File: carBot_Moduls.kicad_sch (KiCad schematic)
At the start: 12 parts, among them J1 Batt_1, J2 Batt_2, J3 Conn_MOT_FL, J4 Conn_MOT_RL, J5 Conn_MOT_FR, J6 Conn_MOT_RR, SW1 SW_SPST

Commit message: Add all modules
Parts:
- added BZ1: Buzzer, symbol Device:Buzzer
- added D1: 1N4148, Diode_THT:D_DO-35_SOD27_P7.62mm_Horizontal, symbol Diode:1N4148
- added J10: IR_sensor, symbol Connector_Generic:Conn_01x03
- added J11: RGB_LED_B, symbol Connector_Generic:Conn_01x03
- added J7: UltraSonic, symbol Connector_Generic:Conn_01x04
- added J8: RGB_LED_F, symbol Connector_Generic:Conn_01x03
- added J9: OLED, symbol Connector_Generic:Conn_01x04
- added Q1: BC547, Package_TO_SOT_THT:TO-92_Inline, symbol Transistor_BJT:BC547
- added R1, R3: 330, symbol Device:R
- added R2: 1K, symbol Device:R
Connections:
- net +5V: now also BZ1.1 (+), D1.1 (K), J11.2 (Pin_2), J8.2 (Pin_2)
- net 3.3V: now also J10.1 (Pin_1), J7.1 (Pin_1), J9.2 (Pin_2)
- net GND: now also J10.2 (Pin_2), J11.3 (Pin_3), J7.4 (Pin_4), J8.3 (Pin_3), J9.1 (Pin_1), Q1.3 (E)
- net SONAR_ECHO: now also J7.3 (Pin_3)
- net SONAR_TRIG: now also J7.2 (Pin_2)
- net IR_DATA: now reaches U1.31 (Pin_31)
- net IR_DATA: now also J10.3 (Pin_3)
- net OLED_SDA: now reaches U1.33 (Pin_33)
- net OLED_SDA: now also J9.4 (Pin_4)
- net OLED_SCL: now reaches U1.36 (Pin_36)
- net OLED_SCL: now also J9.3 (Pin_3)
- net Buzzer_EN: now reaches U1.37 (Pin_37)
- net Buzzer_EN: now also R2.1
- net LED_DATA_B: now reaches U1.7 (Pin_7)
- net LED_DATA_B: now also R3.1
- net LED_DATA renamed LED_DATA_F
- net LED_DATA_F: now also R1.1
- new net: Q1.2 (B), R2.2
- new net: J11.1 (Pin_1), R3.2
- new net: J8.1 (Pin_1), R1.2
- new net: BZ1.2 (-), D1.2 (A), Q1.1 (C)
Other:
- moved on the sheet: C1, J1, J2, J3, J4, J5, J6, SW1, U1, U2, U3, U4

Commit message: Add files via upload
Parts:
- added J12: Conn_01x06, CarBotLibrary:TP4056_TypeC_Module, symbol Connector_Generic:Conn_01x06
- U1: footprint (none) -> CarBotLibrary:ESP32-38pins
- U2: footprint (none) -> CarBotLibrary:Buck
- U3: footprint (none) -> CarBotLibrary:BMS
- U4: footprint (none) -> CarBotLibrary:MotDriver
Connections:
- no-connect marks 0 -> 1
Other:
- moved on the sheet: J10, J9
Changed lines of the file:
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@@
 		(color 0 0 0 0)
 	)
+	(no_connect
+		(at 45.72 74.93)
+	)
 	(wire
 		(pts
@@
 	(wire
 		(pts
-			(xy 230.505 151.13) (xy 233.68 151.13)
+			(xy 231.14 135.89) (xy 234.315 135.89)
 		)
 		(stroke
@@
 	(wire
 		(pts
-			(xy 230.505 153.67) (xy 233.68 153.67)
-		)
-		(stroke
-			(width 0)
-			(type default)
-		)
-	)
-	(wire
-		(pts
-			(xy 230.505 148.59) (xy 233.68 148.59)
+			(xy 231.14 138.43) (xy 234.315 138.43)
+		)
+		(stroke
+			(width 0)
+			(type default)
+		)
+	)
+	(wire
+		(pts
+			(xy 231.14 133.35) (xy 234.315 133.35)
 		)
 		(stroke
@@
 	)
 	(label "IR_DATA"
-		(at 230.505 153.67 180)
+		(at 231.14 138.43 180)
 		(effects
 			(font
@@
 	)
 	(label "GND"
-		(at 230.505 151.13 180)
+		(at 231.14 135.89 180)
 		(effects
 			(font
@@
 	)
 	(label "OLED_SCL"
-		(at 233.68 136.525 180)
+		(at 234.315 121.285 180)
 		(effects
 			(font
@@
 	)
 	(label "3.3V"
-		(at 233.68 133.985 180)
+		(at 234.315 118.745 180)
 		(effects
 			(font
@@
 	)
 	(label "GND"
-		(at 233.68 131.445 180)
+		(at 234.315 116.205 180)
 		(effects
 			(font
@@
 		)
 	)
-	(label "DIN"
-		(at 28.575 73.025 180)
-		(effects
-			(font
-				(size 1.27 1.27)
-			)
-			(justify right bottom)
-		)
-	)
 	(label "3.3V"
-		(at 230.505 148.59 180)
+		(at 231.14 133.35 180)
 		(effects
 			(font
@@
 	)
 	(label "OLED_SDA"
-		(at 233.68 139.065 180)
+		(at 234.315 123.825 180)
 		(effects
 			(font
@@
 	)
 	(symbol
+		(lib_id "Connector_Generic:Conn_01x06")
+		(at 191.135 139.7 0)
+		(unit 1)
+		(exclude_from_sim no)
+		(in_bom yes)
+		(on_board yes)
+		(dnp no)
+		(fields_autoplaced yes)
+		(property "Reference" "J12"
+			(at 194.31 139.6999 0)
+			(effects
+				(font
+					(size 1.27 1.27)
+				)
+				(justify left)
+			)
+		)
+		(property "Value" "Conn_01x06"
+			(at 194.31 142.2399 0)
+			(effects
+				(font
+					(size 1.27 1.27)
+				)
+				(justify left)
+			)
+		)
+		(property "Footprint" "CarBotLibrary:TP4056_TypeC_Module"
+			(at 191.135 139.7 0)
+			(effects
+				(font
+					(size 1.27 1.27)
+				)
+				(hide yes)
+			)
+		)
+		(property "Datasheet" "~"
+			(at 191.135 139.7 0)
+			(effects
+				(font
+					(size 1.27 1.27)
+				)
+				(hide yes)
+			)
+		)
+		(property "Description" "Generic connector, single row, 01x06, script generated (kicad-library-utils/schlib/autogen/connector/)"
+			(at 191.135 139.7 0)
+			(effects
+				(font
+					(size 1.27 1.27)
+				)
+				(hide yes)
+			)
+		)
+		(pin "4"
+		)
+		(pin "2"
+		)
+		(pin "1"
+		)
+		(pin "3"
+		)
+		(pin "5"
+		)
+		(pin "6"
+		)
+		(instances
+			(project ""
+				(path "/df05b431-47a2-405b-9491-3f7c618e89eb"
+					(reference "J12")
+					(unit 1)
+				)
+			)
+		)
+	)
+	(symbol
 		(lib_id "Device:R")
 		(at 144.145 102.87 90)
@@
 			)
 		)
-		(property "Footprint" ""
+		(property "Footprint" "CarBotLibrary:MotDriver"
 			(at 154.305 44.45 0)
 			(effects
@@
 			)
 		)
-		(property "Footprint" ""
+		(property "Footprint" "CarBotLibrary:ESP32-38pins"
 			(at 62.23 29.845 0)
 			(effects
@@
 	(symbol
 		(lib_id "Connector_Generic:Conn_01x03")
-		(at 238.76 151.13 0)
+		(at 239.395 135.89 0)
 		(unit 1)
 		(exclude_from_sim no)
@@
 		(fields_autoplaced yes)
 		(property "Reference" "J10"
-			(at 241.935 149.8599 0)
+			(at 242.57 134.6199 0)
 			(effects
 				(font
@@
 		)
 		(property "Value" "IR_sensor"
-			(at 241.935 152.3999 0)
+			(at 242.57 137.1599 0)
 			(effects
 				(font
@@
 		)
 		(property "Footprint" ""
-			(at 238.76 151.13 0)
+			(at 239.395 135.89 0)
 			(effects
 				(font
@@
 		)
 		(property "Datasheet" "~"
-			(at 238.76 151.13 0)
+			(at 239.395 135.89 0)
 			(effects
 				(font
@@
 		)
 		(property "Description" "Generic connector, single row, 01x03, script generated (kicad-library-utils/schlib/autogen/connector/)"
-			(at 238.76 151.13 0)
+			(at 239.395 135.89 0)
 			(effects
 				(font
@@
 	(symbol
 		(lib_id "Connector_Generic:Conn_01x04")
-		(at 238.76 133.985 0)
+		(at 239.395 118.745 0)
 		(unit 1)
 		(exclude_from_sim no)
@@
 		(fields_autoplaced yes)
 		(property "Reference" "J9"
-			(at 241.3 133.9849 0)
+			(at 241.935 118.7449 0)
 			(effects
 				(font
@@
 		)
 		(property "Value" "OLED"
-			(at 241.3 136.5249 0)
+			(at 241.935 121.2849 0)
 			(effects
 				(font
@@
 		)
 		(property "Footprint" ""
-			(at 238.76 133.985 0)
+			(at 239.395 118.745 0)
 			(effects
 				(font
@@
 		)
 		(property "Datasheet" "~"
-			(at 238.76 133.985 0)
+			(at 239.395 118.745 0)
 			(effects
 				(font
@@
 		)
 		(property "Description" "Generic connector, single row, 01x04, script generated (kicad-library-utils/schlib/autogen/connector/)"
-			(at 238.76 133.985 0)
+			(at 239.395 118.745 0)
 			(effects
 				(font
@@
 			)
 		)
-		(property "Footprint" ""
+		(property "Footprint" "CarBotLibrary:BMS"
 			(at 213.36 17.145 0)
 			(effects
@@
 					(size 1.27 1.27)
 				)
-			)
-		)
-		(property "Footprint" ""
+				(hide yes)
+			)
+		)
+		(property "Footprint" "CarBotLibrary:Buck"
 			(at 172.72 18.415 0)
 			(effects

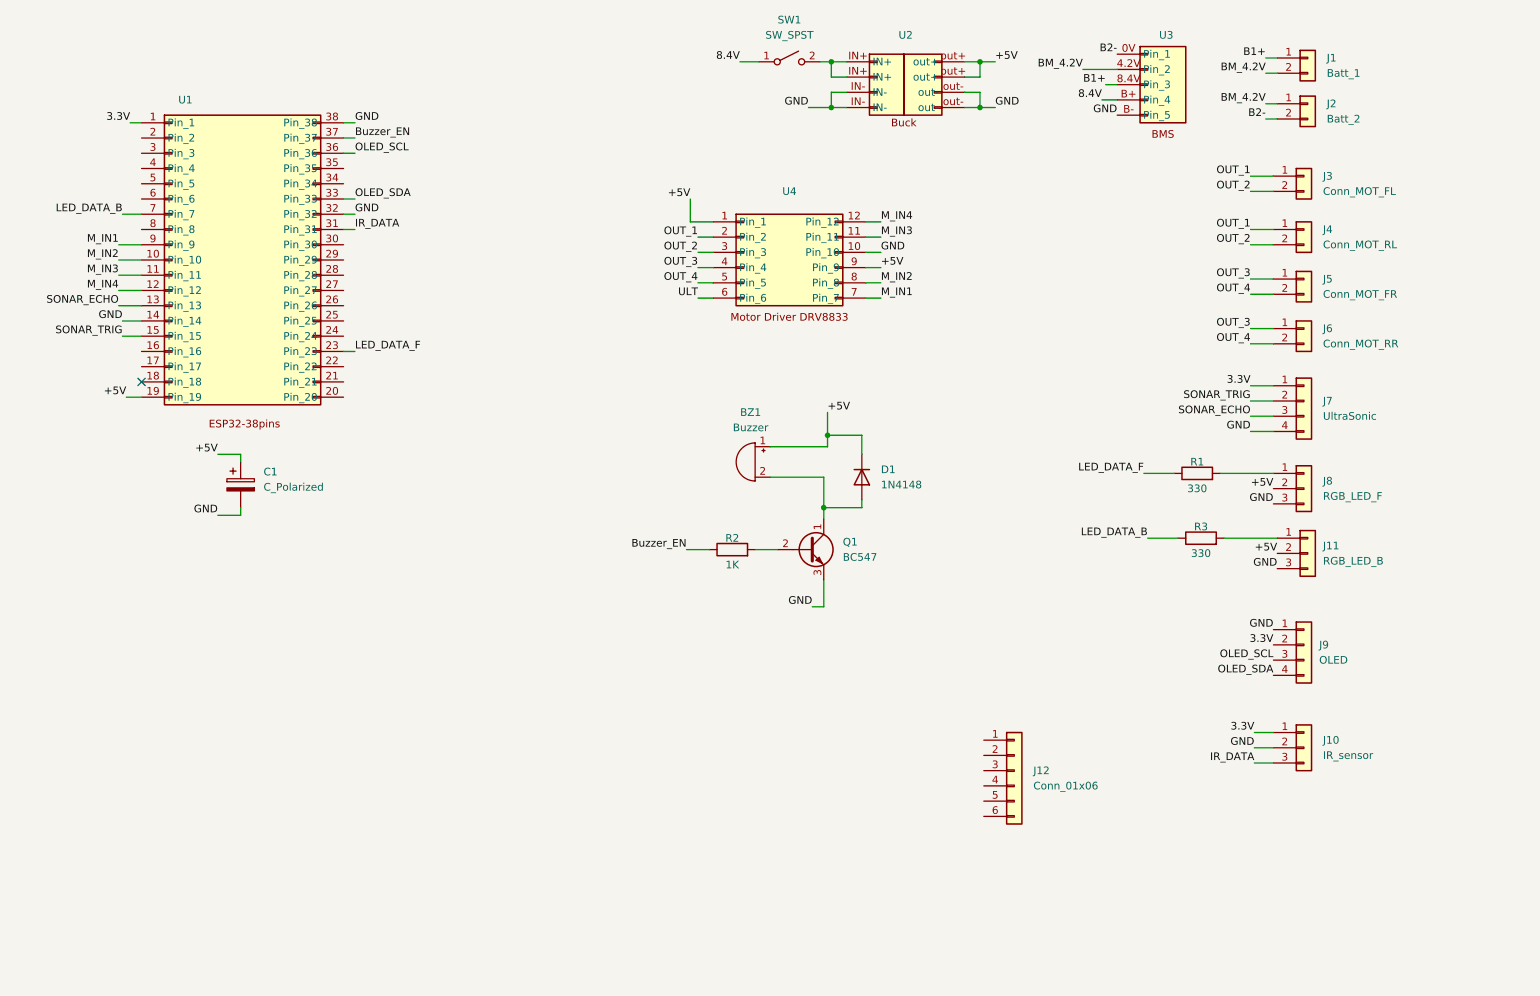
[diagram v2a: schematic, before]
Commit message: assgin footprint
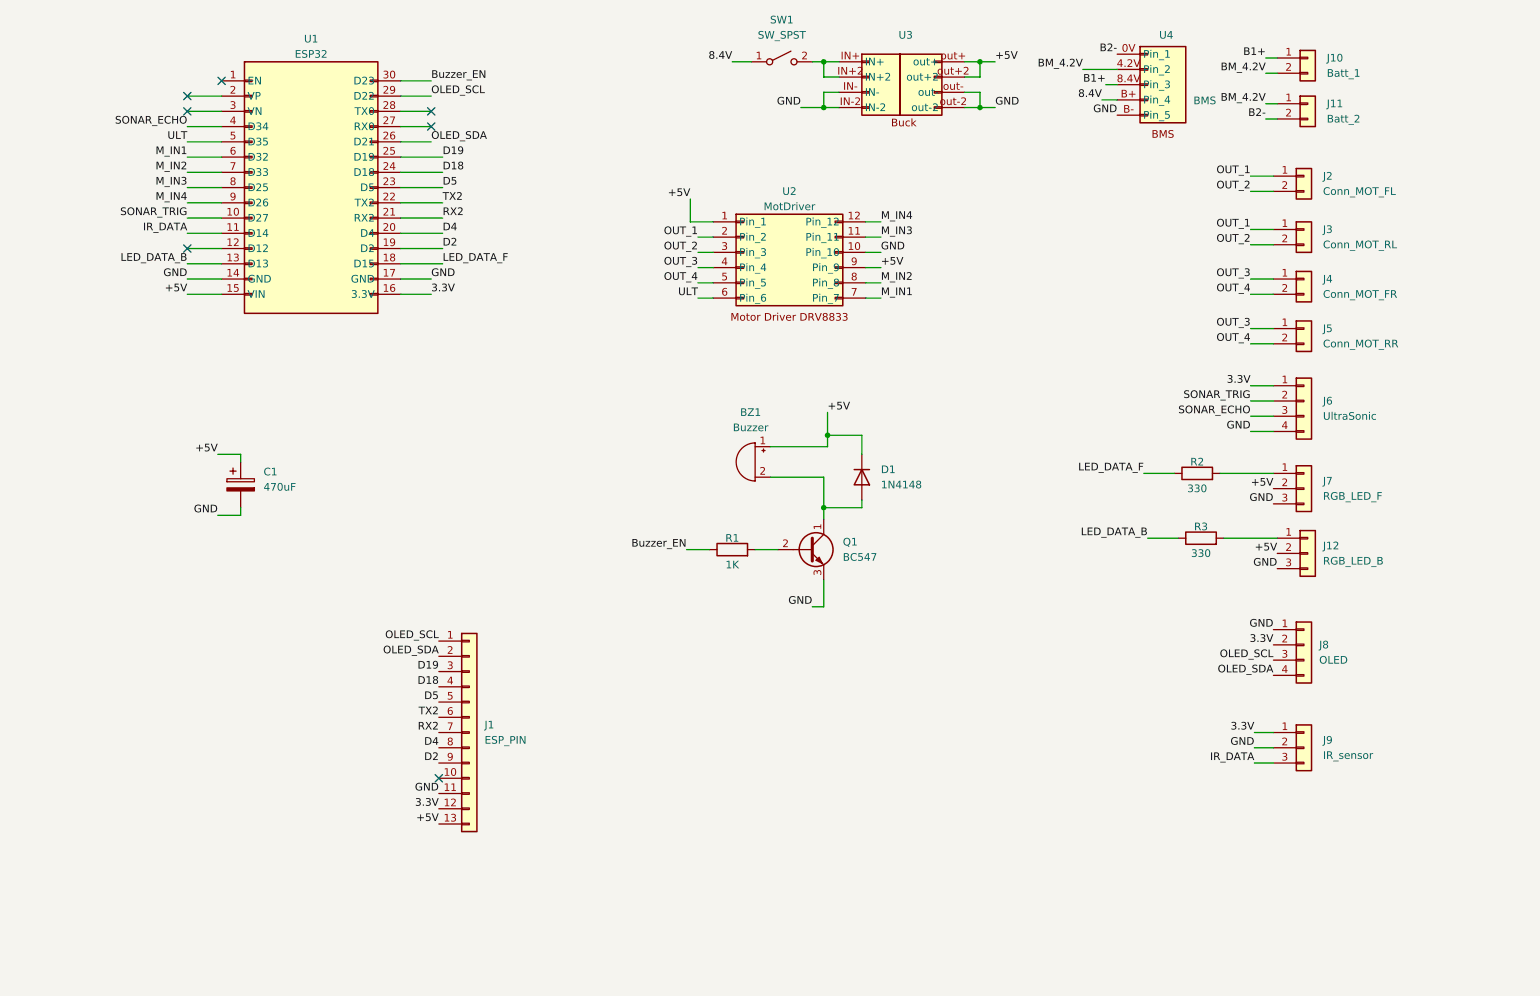
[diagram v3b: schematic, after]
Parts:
- removed J12: Conn_01x06, CarBotLibrary:TP4056_TypeC_Module, symbol Connector_Generic:Conn_01x06
- removed U1: ~, CarBotLibrary:ESP32-38pins, symbol CarBot:ESP32-38pins
- added J1: ESP_PIN, Connector_PinHeader_2.54mm:PinHeader_1x13_P2.54mm_Vertical, symbol Connector_Generic:Conn_01x13
- added U1: ESP32, CarBotLibrary:ESP32-30pins, symbol CarBot:ESP32-30PINS
- BZ1: footprint (none) -> Buzzer_Beeper:Buzzer_12x9.5RM7.6
- C1: value C_Polarized -> 470uF; footprint (none) -> Capacitor_THT:CP_Radial_D5.0mm_P2.50mm
- J10: renamed from J1; footprint (none) -> Connector_JST:JST_XH_B2B-XH-A_1x02_P2.50mm_Vertical
- J11: renamed from J2; footprint (none) -> Connector_JST:JST_XH_B2B-XH-A_1x02_P2.50mm_Vertical
- J12: renamed from J11; footprint (none) -> Connector_JST:JST_XH_B3B-XH-A_1x03_P2.50mm_Vertical
- J2: renamed from J3; footprint (none) -> Connector_JST:JST_XH_B2B-XH-A_1x02_P2.50mm_Vertical
- J3: renamed from J4; footprint (none) -> Connector_JST:JST_XH_B2B-XH-A_1x02_P2.50mm_Vertical
- J4: renamed from J5; footprint (none) -> Connector_JST:JST_XH_B2B-XH-A_1x02_P2.50mm_Vertical
- J5: renamed from J6; footprint (none) -> Connector_JST:JST_XH_B2B-XH-A_1x02_P2.50mm_Vertical
- J6: renamed from J7; footprint (none) -> Connector_JST:JST_XH_B4B-XH-A_1x04_P2.50mm_Vertical
- J7: renamed from J8; footprint (none) -> Connector_JST:JST_XH_B3B-XH-A_1x03_P2.50mm_Vertical
- J8: renamed from J9; footprint (none) -> Connector_JST:JST_XH_B4B-XH-A_1x04_P2.50mm_Vertical
- J9: renamed from J10; footprint (none) -> Connector_JST:JST_XH_B3B-XH-A_1x03_P2.50mm_Vertical
- R1: renamed from R2; footprint (none) -> Resistor_THT:R_Axial_DIN0204_L3.6mm_D1.6mm_P7.62mm_Horizontal
- R2: renamed from R1; footprint (none) -> Resistor_THT:R_Axial_DIN0204_L3.6mm_D1.6mm_P7.62mm_Horizontal
- R3: footprint (none) -> Resistor_THT:R_Axial_DIN0204_L3.6mm_D1.6mm_P7.62mm_Horizontal
- SW1: footprint (none) -> CarBotLibrary:KCD1-11_ON_OFF
- U2: renamed from U4; value ~ -> MotDriver
- U3: renamed from U2; value ~ -> Buck
- U4: renamed from U3; value ~ -> BMS
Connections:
- net +5V: now also U3.out+2, J1.13 (Pin_13), U1.15 (VIN)
- net 3.3V: now also J1.12 (Pin_12), U1.16 (3.3V)
- net Buzzer_EN: now also U1.30 (D23)
- net GND: now also U3.IN-2, U3.out-2, J1.11 (Pin_11), U1.14 (GND), U1.17 (GND)
- net IR_DATA: now also U1.11 (D14)
- net LED_DATA_B: now also U1.13 (D13)
- net LED_DATA_F: now also U1.18 (D15)
- net M_IN1: now also U1.6 (D32)
- net M_IN2: now also U1.7 (D33)
- net M_IN3: now also U1.8 (D25)
- net M_IN4: now also U1.9 (D26)
- net OLED_SCL: now also J1.1 (Pin_1), U1.29 (D22)
- net OLED_SDA: now also J1.2 (Pin_2), U1.26 (D21)
- net SONAR_ECHO: now also U1.4 (D34)
- net SONAR_TRIG: now also U1.10 (D27)
- net ULT: now also U1.5 (D35)
- net at SW1.2 (B), U3.IN+: now also U3.IN+2
- new net D18: J1.4 (Pin_4), U1.24 (D18)
- new net D19: J1.3 (Pin_3), U1.25 (D19)
- new net D2: J1.9 (Pin_9), U1.19 (D2)
- new net D4: J1.8 (Pin_8), U1.20 (D4)
- new net D5: J1.5 (Pin_5), U1.23 (D5)
- new net RX2: J1.7 (Pin_7), U1.21 (RX2)
- new net TX2: J1.6 (Pin_6), U1.22 (TX2)
- no-connect marks 1 -> 7
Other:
- moved on the sheet: SW1, U3

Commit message: Routing and generate Gerber
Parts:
- added D2: Power_ON, LED_THT:LED_D3.0mm, symbol Device:LED
- added D3: LED (Blue, Green), LED_THT:LED_D3.0mm, symbol Device:LED
- added H1, H2, H3: ~, MountingHole:MountingHole_3mm, symbol Mechanical:MountingHole
- added R4: 1K, Resistor_THT:R_Axial_DIN0204_L3.6mm_D1.6mm_P7.62mm_Horizontal, symbol Device:R
- added R5: 10K, Resistor_THT:R_Axial_DIN0204_L3.6mm_D1.6mm_P7.62mm_Horizontal, symbol Device:R
- added R6: 330, Resistor_THT:R_Axial_DIN0204_L3.6mm_D1.6mm_P7.62mm_Horizontal, symbol Device:R
- added SW2: B1, Button_Switch_THT:SW_PUSH_6mm, symbol Switch:SW_Push
- J2: value Conn_MOT_FL -> Conn_MOT_FR
- J3: value Conn_MOT_RL -> Conn_MOT_RR
- J4: value Conn_MOT_FR -> Conn_MOT_FL
- J5: value Conn_MOT_RR -> Conn_MOT_RL
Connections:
- net +5V: now also J1.11 (Pin_11), R4.1; no longer J1.13 (Pin_13)
- net 3.3V: now also J1.13 (Pin_13), R5.2, R6.1; no longer J1.12 (Pin_12)
- net Buzzer_EN: now also U1.5 (D35); no longer U1.30 (D23)
- net GND: now also J1.10 (Pin_10), J1.12 (Pin_12), D2.1 (K), SW2.1; no longer J1.11 (Pin_11)
- net IR_DATA: now also U1.4 (D34); no longer U1.11 (D14)
- net SONAR_ECHO: now also U1.10 (D27); no longer U1.4 (D34)
- net SONAR_TRIG: now also U1.11 (D14); no longer U1.10 (D27)
- net user_led: now reaches U1.12 (D12)
- net user_led: now also D3.1 (K)
- net user_button: now reaches U1.28 (TX0)
- net user_button: now also R5.1, SW2.2
- net ULT: no longer names the net of U2.6 (Pin_6)
- net ULT: no longer U1.5 (D35)
- new net: D2.2 (A), R4.2
- new net: D3.2 (A), R6.2
- no-connect marks 7 -> 6
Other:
- note added: "User Led + Button"
- moved on the sheet: J1, SW1, U2, U3

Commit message: Add carbot modules-v2
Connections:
- net Buzzer_EN: now also U1.19 (D2); no longer U1.5 (D35)
- net D2: no longer U1.19 (D2)
- no-connect marks 6 -> 7
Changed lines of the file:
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@@
+	)
+	(no_connect
+		(at 53.34 34.925)
 	)
 	(no_connect
@@
 	)
 	(label "Buzzer_EN"
-		(at 53.34 34.925 180)
-		(effects
-			(font
-				(size 1.27 1.27)
-			)
-			(justify right bottom)
+		(at 95.885 52.705 0)
+		(effects
+			(font
+				(size 1.27 1.27)
+			)
+			(justify left bottom)
 		)
 	)
@@
 		)
 	)
-	(label "D2"
-		(at 95.885 52.705 0)
-		(effects
-			(font
-				(size 1.27 1.27)
-			)
-			(justify left bottom)
-		)
-	)
